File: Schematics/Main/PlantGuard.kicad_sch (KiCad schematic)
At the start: 7 parts, among them M1 Motor_DC, SW1 SW_SP3T, U1 L298N, U2 LM78M05_TO252

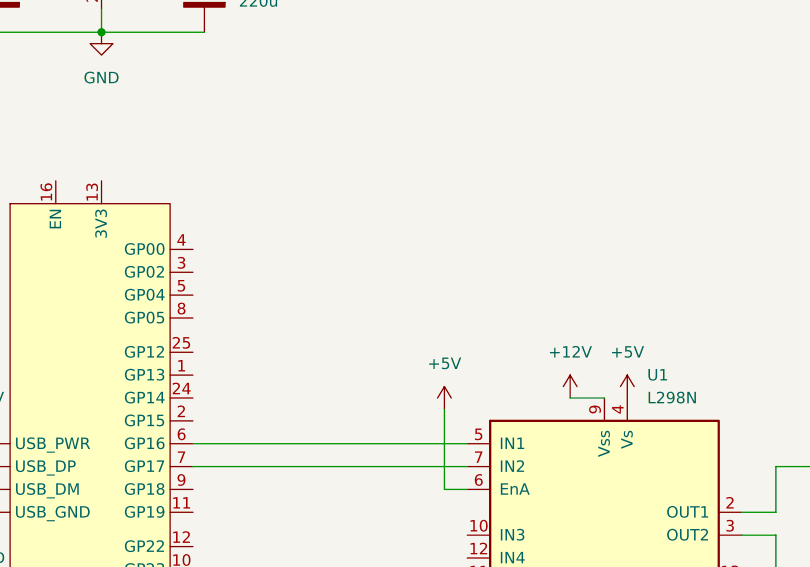
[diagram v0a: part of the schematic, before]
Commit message: Connect the motorized valve
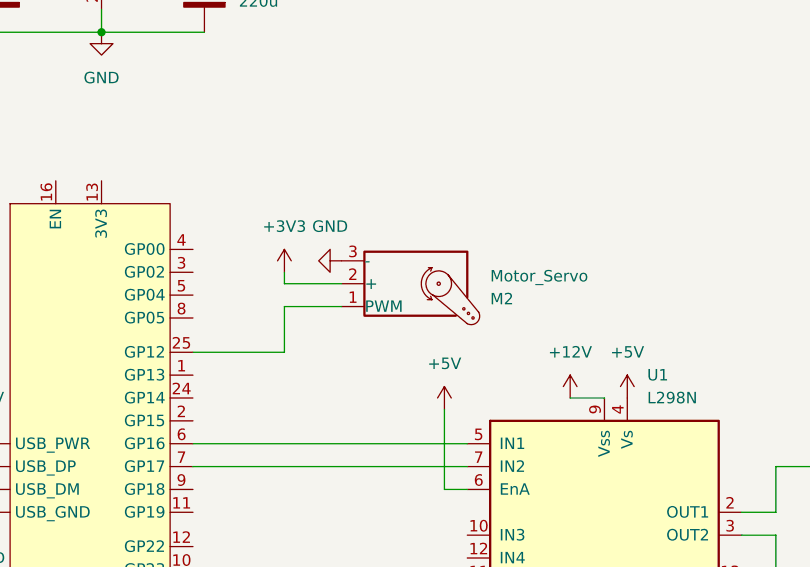
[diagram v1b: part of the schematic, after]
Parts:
- added M2: Motor_Servo, symbol Motor:Motor_Servo
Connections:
- net GND: now also M2.3 (-)
- net at U3.25 (GP12): now also M2.1 (PWM)
- new net +3V3: M2.2 (+)
